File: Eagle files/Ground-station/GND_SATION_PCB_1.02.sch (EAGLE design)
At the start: 60 parts, among them IC1 BMP280, J1 USB4110GFA, J3 B4B-XH-AM_(LF)(SN), J6 503182-1852, U1 AMS1117-5.0, U2 SOIC127P790X216-8NW25Q128JVJSQ, U3 AMS1117-3.3

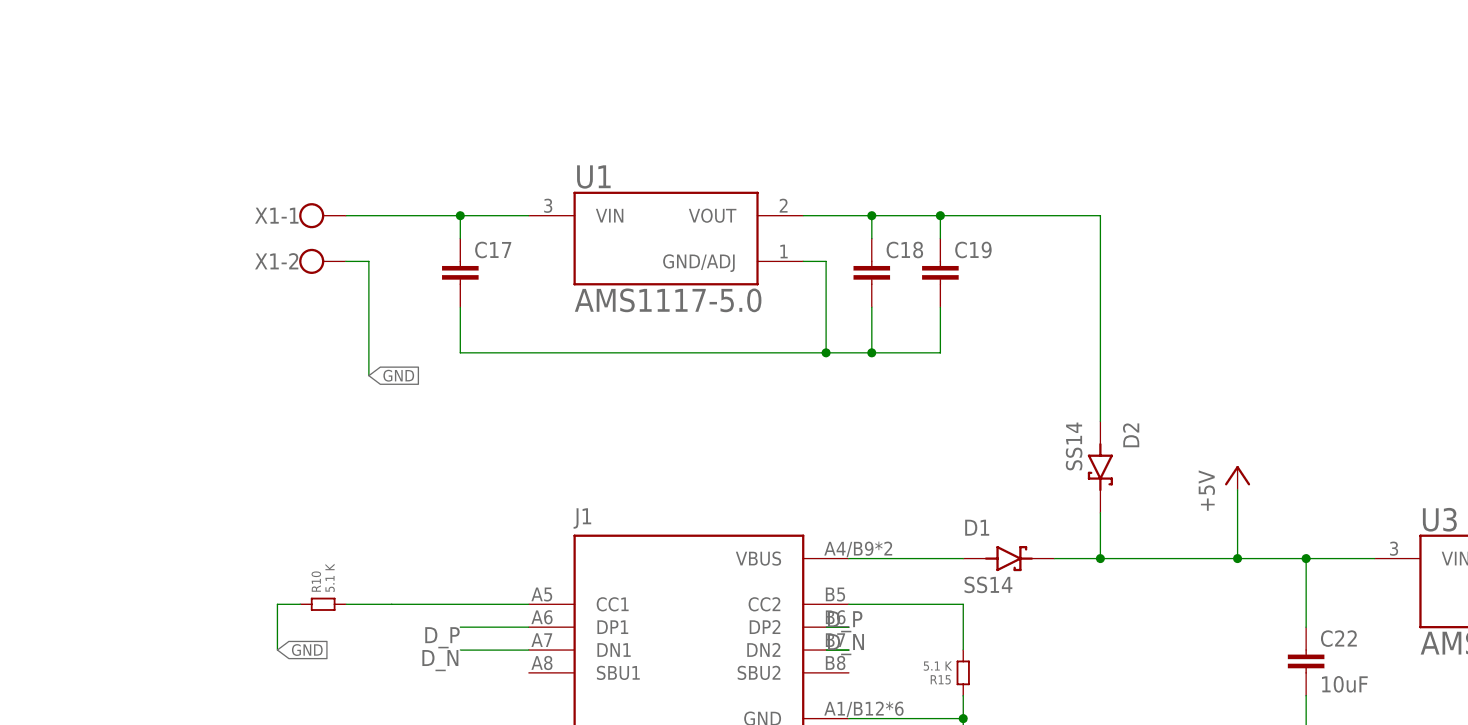
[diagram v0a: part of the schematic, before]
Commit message: Refined power supply design for 5V and added the XT60 M connector
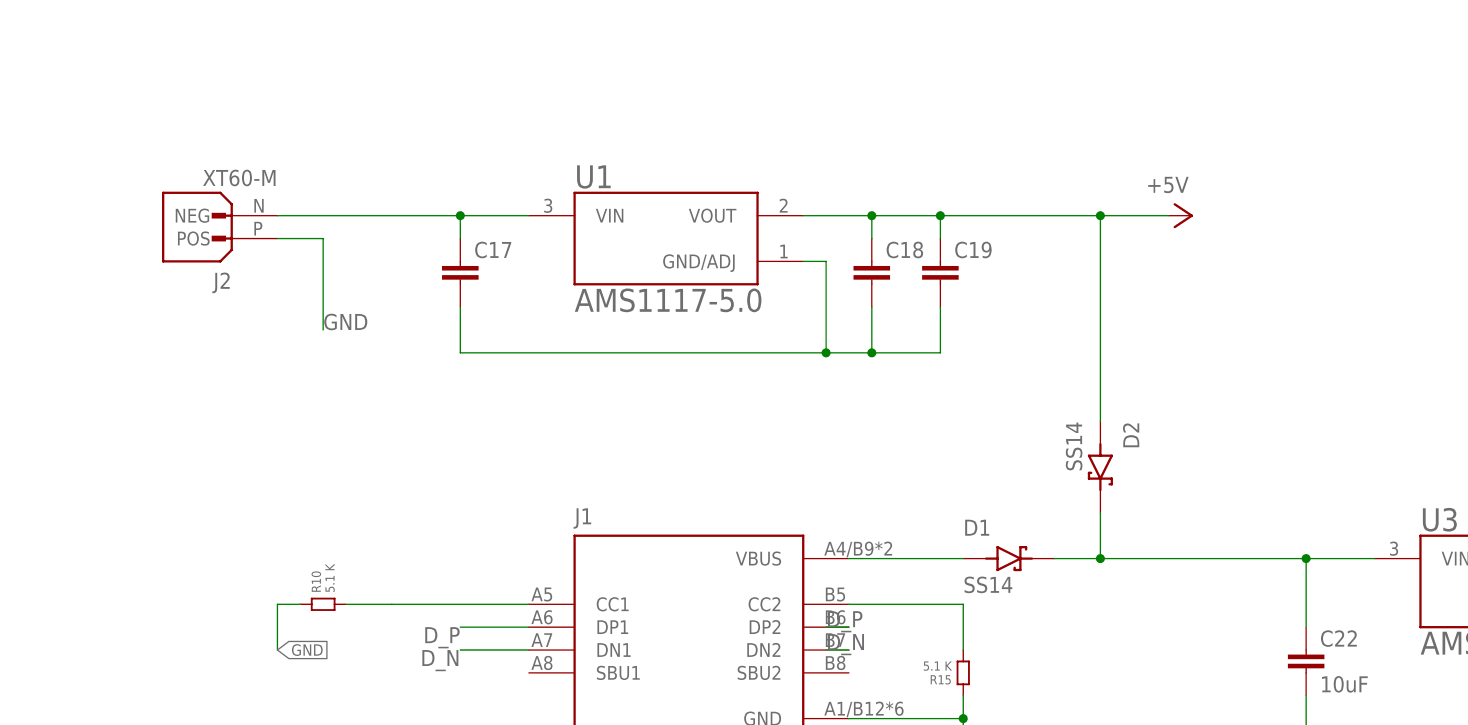
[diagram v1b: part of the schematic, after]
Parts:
- removed X1: (no value), con-wago-500:W237-102
- added J2: XT60-M, XT60-M:XT60-M
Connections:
- removed net N$10: C18.1, C19.1, D2.A, U1.VOUT
- new net N$17: C22.1, D1.K, D2.K, U3.VIN
- net +5V: now also C18.1, C19.1, D2.A, U1.VOUT; no longer C22.1, D1.K, D2.K, U3.VIN
- net GND: now also J2.POS; no longer X1-2.KL
- net N$16: now also J2.NEG; no longer X1-1.KL
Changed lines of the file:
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@@
 <?xml version="1.0" encoding="utf-8"?>
 <!DOCTYPE eagle SYSTEM "eagle.dtd">
-<eagle version="9.7.0">
+<eagle version="9.6.2">
 <drawing>
 <settings>
@@
 <part name="C19" library="rcl" library_urn="urn:adsk.eagle:library:334" deviceset="C-EU" device="C0603" package3d_urn="urn:adsk.eagle:package:23616/2"/>
 <part name="D2" library="SS14" deviceset="SS14" device=""/>
-<part name="P+1" library="supply1" library_urn="urn:adsk.eagle:library:371" deviceset="+5V" device=""/>
-<part name="X1" library="con-wago-500" library_urn="urn:adsk.eagle:library:195" deviceset="W237-102" device="" package3d_urn="urn:adsk.eagle:package:10688/1"/>
 <part name="LCD" library="microbuilder" deviceset="HEADER-1X9" device=""/>
 <part name="R1" library="standardparts" deviceset="RESISTOR" device=".0603" value="10k ohm"/>
@@
 <part name="R10" library="standardparts" deviceset="RESISTOR" device=".0603" value="5.1 K"/>
 <part name="R15" library="standardparts" deviceset="RESISTOR" device=".0603" value="5.1 K"/>
+<part name="P+1" library="supply1" library_urn="urn:adsk.eagle:library:371" deviceset="+5V" device=""/>
+<part name="J2" library="XT60-M" deviceset="XT60-M" device=""/>
 </parts>
 <sheets>
@@
 <attribute name="VALUE" x="-1.27" y="-78.74" size="1.778" layer="96" rot="R270"/>
 </instance>
-<instance part="P+1" gate="1" x="17.78" y="-83.82" smashed="yes">
-<attribute name="VALUE" x="15.24" y="-88.9" size="1.778" layer="96" rot="R90"/>
-</instance>
-<instance part="X1" gate="-1" x="-86.36" y="-55.88" smashed="yes">
-<attribute name="NAME" x="-86.36" y="-54.991" size="1.778" layer="95" rot="R180"/>
-</instance>
-<instance part="X1" gate="-2" x="-86.36" y="-60.96" smashed="yes">
-<attribute name="VALUE" x="-88.9" y="-64.643" size="1.778" layer="96"/>
-<attribute name="NAME" x="-86.36" y="-60.071" size="1.778" layer="95" rot="R180"/>
-</instance>
 <instance part="LCD" gate="A" x="-330.2" y="134.62" smashed="yes">
 <attribute name="NAME" x="-336.55" y="147.955" size="1.778" layer="95"/>
@@
 <attribute name="NAME" x="-13.97" y="-107.95" size="1.016" layer="95" rot="MR0"/>
 <attribute name="VALUE" x="-13.97" y="-105.41" size="1.016" layer="96" rot="R180"/>
+</instance>
+<instance part="P+1" gate="1" x="12.7" y="-55.88" smashed="yes" rot="R270">
+<attribute name="VALUE" x="7.62" y="-53.34" size="1.778" layer="96"/>
+</instance>
+<instance part="J2" gate="G$1" x="-93.98" y="-55.88" smashed="yes" rot="R180">
+<attribute name="NAME" x="-93.98" y="-62.23" size="1.778" layer="95" rot="R180"/>
+<attribute name="VALUE" x="-88.9" y="-50.8" size="1.778" layer="96" rot="R180"/>
 </instance>
 </instances>
@@
 </segment>
 <segment>
-<pinref part="X1" gate="-2" pin="KL"/>
-<wire x1="-81.28" y1="-60.96" x2="-78.74" y2="-60.96" width="0.1524" layer="91"/>
-<wire x1="-78.74" y1="-60.96" x2="-78.74" y2="-73.66" width="0.1524" layer="91"/>
-<label x="-78.74" y="-73.66" size="1.27" layer="95" xref="yes"/>
-</segment>
-<segment>
 <wire x1="-86.36" y1="-99.06" x2="-88.9" y2="-99.06" width="0.1524" layer="91"/>
 <wire x1="-88.9" y1="-99.06" x2="-88.9" y2="-104.14" width="0.1524" layer="91"/>
@@
 <wire x1="63.5" y1="-114.3" x2="63.5" y2="-116.84" width="0.1524" layer="91"/>
 <label x="63.5" y="-119.38" size="1.27" layer="95" xref="yes"/>
+</segment>
+<segment>
+<pinref part="J2" gate="G$1" pin="POS"/>
+<wire x1="-88.9" y1="-58.42" x2="-83.82" y2="-58.42" width="0.1524" layer="91"/>
+<wire x1="-83.82" y1="-58.42" x2="-83.82" y2="-68.58" width="0.1524" layer="91"/>
+<label x="-83.82" y="-68.58" size="1.778" layer="95"/>
 </segment>
 </net>
@@
 </segment>
 </net>
-<net name="+5V" class="0">
-<segment>
-<pinref part="D1" gate="G$1" pin="K"/>
-<pinref part="U3" gate="G$1" pin="VIN"/>
-<wire x1="33.02" y1="-93.98" x2="25.4" y2="-93.98" width="0.1524" layer="91"/>
-<wire x1="25.4" y1="-93.98" x2="17.78" y2="-93.98" width="0.1524" layer="91"/>
-<wire x1="17.78" y1="-93.98" x2="2.54" y2="-93.98" width="0.1524" layer="91"/>
-<wire x1="2.54" y1="-93.98" x2="-2.54" y2="-93.98" width="0.1524" layer="91"/>
-<wire x1="25.4" y1="-93.98" x2="25.4" y2="-101.6" width="0.1524" layer="91"/>
-<junction x="25.4" y="-93.98"/>
-<pinref part="C22" gate="G$1" pin="1"/>
-<wire x1="2.54" y1="-93.98" x2="2.54" y2="-88.9" width="0.1524" layer="91"/>
-<junction x="2.54" y="-93.98"/>
-<pinref part="D2" gate="G$1" pin="K"/>
-<wire x1="17.78" y1="-93.98" x2="17.78" y2="-86.36" width="0.1524" layer="91"/>
-<junction x="17.78" y="-93.98"/>
-<pinref part="P+1" gate="1" pin="+5V"/>
-</segment>
-</net>
 <net name="N$14" class="0">
 <segment>
@@
 </segment>
 </net>
-<net name="N$10" class="0">
+<net name="+5V" class="0">
 <segment>
 <pinref part="U1" gate="G$1" pin="VOUT"/>
@@
 <wire x1="2.54" y1="-55.88" x2="2.54" y2="-78.74" width="0.1524" layer="91"/>
 <junction x="-15.24" y="-55.88"/>
+<wire x1="2.54" y1="-55.88" x2="10.16" y2="-55.88" width="0.1524" layer="91"/>
+<junction x="2.54" y="-55.88"/>
+<pinref part="P+1" gate="1" pin="+5V"/>
 </segment>
 </net>
@@
 <pinref part="C17" gate="G$1" pin="1"/>
 <wire x1="-68.58" y1="-55.88" x2="-68.58" y2="-58.42" width="0.1524" layer="91"/>
-<wire x1="-68.58" y1="-55.88" x2="-81.28" y2="-55.88" width="0.1524" layer="91"/>
+<wire x1="-68.58" y1="-55.88" x2="-88.9" y2="-55.88" width="0.1524" layer="91"/>
 <junction x="-68.58" y="-55.88"/>
-<pinref part="X1" gate="-1" pin="KL"/>
+<pinref part="J2" gate="G$1" pin="NEG"/>
 </segment>
 </net>
@@
 </segment>
 </net>
+<net name="N$17" class="0">
+<segment>
+<pinref part="D1" gate="G$1" pin="K"/>
+<pinref part="U3" gate="G$1" pin="VIN"/>
+<wire x1="33.02" y1="-93.98" x2="25.4" y2="-93.98" width="0.1524" layer="91"/>
+<wire x1="25.4" y1="-93.98" x2="2.54" y2="-93.98" width="0.1524" layer="91"/>
+<wire x1="2.54" y1="-93.98" x2="-2.54" y2="-93.98" width="0.1524" layer="91"/>
+<wire x1="25.4" y1="-93.98" x2="25.4" y2="-101.6" width="0.1524" layer="91"/>
+<junction x="25.4" y="-93.98"/>
+<pinref part="C22" gate="G$1" pin="1"/>
+<wire x1="2.54" y1="-93.98" x2="2.54" y2="-88.9" width="0.1524" layer="91"/>
+<junction x="2.54" y="-93.98"/>
+<pinref part="D2" gate="G$1" pin="K"/>
+</segment>
+</net>

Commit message: Added buttons
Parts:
- added CN1, CN2, CN3: (no value), microbuilder:HEADER_1X02
- added R16, R20, R21: 1k, rcl:R-EU_R0603
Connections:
- removed net +5V: C18.1, C19.1, D2.A, U1.VOUT
- removed net 5V5: J3.2
- removed net FIN_1: RP2040.GPIO7
- new net 0: R16.1, R20.1, R21.1
- new net 3V3_OUT: CN1.1, RP2040.GPIO24
- new net 5V_OUT: C18.1, C19.1, D2.A, J3.2, U1.VOUT
- new net N$10: CN1.2, CN2.1, CN3.1, R16.2
- new net N$18: CN3.2, R20.2, RP2040.GPIO20
- new net N$19: CN2.2, R21.2, RP2040.GPIO21
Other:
- moved on the sheet: S1

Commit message: .
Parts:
- added C21, C25, C26: 10uF, rcl:C-EUC0603
- added C27, C28, C29: (no value), rcl:C-EUC0603
- added D3, D4: SS14, SS14:SS14
- added J4: USB4110GFA, USB4110GFA:USB4110GFA
- added J5: XT60-M, XT60-M:XT60-M
- added R22, R23: 5.1 K, standardparts:RESISTOR.0603
- added R24: 10k ohm, standardparts:RESISTOR.0603
- added U4: SOIC127P790X216-8NW25Q128JVJSQ, SOIC127P790X216-8N:SOIC127P790X216-8NW25Q128JVJSQ
- added U5: AMS1117-3.3, AMS1117-3.3:AMS1117-3.3
- added U6: AMS1117-5.0, AMS1117-5.0:AMS1117-5.0
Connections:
- new net FLASH_CLK: U4.CLK
- new net FLASH_CS: R24.1, U4./CS
- new net FLASH_DI: U4.DI(IO0)
- new net FLASH_DO: U4.DO(I01)
- new net N$13: J4.CC1, R22.2
- new net N$20: J4.CC2, R23.2
- new net N$21: D3.A, J4.VBUS
- new net N$22: C27.2, C28.2, C29.2, U6.GND/ADJ
- new net N$23: C27.1, J5.NEG, U6.VIN
- new net N$24: C21.1, D3.K, D4.K, U5.VIN
- net 3V3: now also C25.1, C26.1, R24.2, U4./HOLD(IO3), U4./WP(IO2), U4.VCC, U5.VOUT
- net 5V_OUT: now also C28.1, C29.1, D4.A, U6.VOUT
- net D_N: now also J4.DN1, J4.DN2
- net D_P: now also J4.DP1, J4.DP2
- net GND: now also C21.2, C25.2, C26.2, J4.GND, J5.POS, R22.1, R23.1, U4.GND, U5.GND/ADJ
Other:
- note added: "Mismatch in footprint and actual chip"
- note added: "REDO"
- moved on the sheet: C1, C10, C11, C115, C12, C13, C14, C15, C16, C17, C18, C19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

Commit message: revision 1
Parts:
- removed C23, C24, C25, C26: 10uF, rcl:C-EUC0603
- removed C27, C28, C29: (no value), rcl:C-EUC0603
- removed D2, D3, D4: SS14, SS14:SS14
- removed J4: USB4110GFA, USB4110GFA:USB4110GFA
- removed J5: XT60-M, XT60-M:XT60-M
- removed R15, R23: 5.1 K, standardparts:RESISTOR.0603
- removed R19: 10k ohm, standardparts:RESISTOR.0603
- removed S1: DTS-3, DTS-3:DTS-3
- removed U2: SOIC127P790X216-8NW25Q128JVJSQ, SOIC127P790X216-8N:SOIC127P790X216-8NW25Q128JVJSQ
- removed U5: AMS1117-3.3, AMS1117-3.3:AMS1117-3.3
- removed U6: AMS1117-5.0, AMS1117-5.0:AMS1117-5.0
- added S3: DTS-3, DTS-3:DTS-3
- added U$3: ASE, crystal:ASE
- C1, C2: device ngspice-simulation:C -> rcl:C-EUC0805
- C13, C14, C21, C22: device rcl:C-EUC0603 -> rcl:C-EUC0805
- C17, C18, C19: value (none) -> 10uF; device rcl:C-EUC0603 -> rcl:C-EUC0805
- C3: value 100nF -> 10uF; device rcl:C-EUC0603 -> rcl:C-EUC0805
- R10: value 5.1 K -> 5.1k; device standardparts:RESISTOR.0603 -> rcl:R-EU_R0805
- R22: value 5.1 K -> 10k; device standardparts:RESISTOR.0603 -> rcl:R-EU_R0805
- R6: value 10k ohm -> 10k; device standardparts:RESISTOR.0603 -> rcl:R-EU_R0805
- R7: value 10k ohm -> 5.1k; device standardparts:RESISTOR.0603 -> rcl:R-EU_R0805
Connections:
- removed net N$11: J1.CC1, R10.2
- removed net N$13: J4.CC1, R22.2
- removed net N$17: C22.1, D1.K, D2.K, U3.VIN
- removed net N$20: J4.CC2, R23.2
- removed net N$21: D3.A, J4.VBUS
- removed net N$22: C27.2, C28.2, C29.2, U6.GND/ADJ
- removed net N$23: C27.1, J5.NEG, U6.VIN
- removed net N$24: C21.1, D3.K, D4.K, U5.VIN
- net +3V3: no longer C3.1, R7.2, U2.VCC
- net 3V3: now also C1.2, C19.1, C21.1; no longer C1.1, C23.1, C24.1, C25.1, C26.1, U5.VOUT
- net 5V_OUT: now also C17.1, C22.1, C3.1, U3.VIN; no longer C18.1, C19.1, C28.1, C29.1, D2.A, D4.A, U6.VOUT
- net D_N: no longer J4.DN1, J4.DN2
- net D_P: no longer J4.DP1, J4.DP2
- net FLASH_CS: now also R22.2
- net GND: now also C1.1, C17.2, C18.2, C19.2, J2.NEG, R7.1, S3.1, U1.GND/ADJ; no longer C1.2, C23.2, C24.2, C25.2, C26.2, J2.POS, J4.GND, J5.POS, R15.1, R22.1, R23.1, S1.1, U2.GND, U5.GND/ADJ
- net N$15: now also R10.2; no longer R15.2
- net N$16: now also C18.1, J2.POS; no longer C17.1, J2.NEG
- net N$2: now also R22.1, S3.2; no longer C17.2, C18.2, C19.2, U1.GND/ADJ
- net N$4: now also C14.2; no longer C13.2
- net N$5: now also J1.CC1, R7.2; no longer R19.1, S1.2
- net QSPI_SCLK: no longer U2.CLK
- net QSPI_SD0: no longer U2.DI(IO0)
- net QSPI_SD1: no longer U2.DO(I01)
- net QSPI_SD2: no longer U2./WP(IO2)
- net QSPI_SD3: no longer U2./HOLD(IO3)
- net QSPI_SS: no longer R19.2, R7.1, U2./CS
- net XIN: now also C13.2; no longer C14.2
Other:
- note added: "Crystal Oscillator"
- note added: "Flash chip (W25Q125JV)"
- note added: "Power Supply"
- moved on the sheet: C1, C13, C14, C17, C18, C19, C2, C21, C3, IC1, J2, R24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

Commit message: Revision 1.01
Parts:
- removed C13, C14: 15pF, rcl:C-EUC0805
- removed R24: 10k ohm, standardparts:RESISTOR.0603
- removed R6: 10k, rcl:R-EU_R0805
- removed U$1: ABM8-272-T3, ABM8-272-T3:ABM8-272-T3
- added C23, C24: 18pF, rcl:C-EUC0805
- added R15: 1k, rcl:R-EU_R0805
- added R19: 10k, rcl:R-EU_R0805
- R22: value 10k -> 1k
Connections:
- removed net N$4: C14.2, R6.1, U$1.3
- new net N$11: C23.1, R15.1, U$3.OUT
- net 3V3: now also R19.2; no longer R24.2
- net FLASH_CS: now also R19.1; no longer R24.1
- net GND: now also C23.2, C24.1, U$3.GND, U$3.VDD; no longer C13.1, C14.1, U$1.2, U$1.4
- net XIN: now also R15.2; no longer C13.2, U$1.1
- net XOUT: now also C24.2, U$3.TRI; no longer R6.2
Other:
- note added: "Use YSX321SL 12pF 10PPM oscillator. If of different load resistance change the C23 and C24."
- moved on the sheet: U$3
